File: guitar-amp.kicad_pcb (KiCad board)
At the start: 2 copper layers, 135 x 90 mm, 72 parts, among them J1 Speaker Output, J2 Input, J3 AC Mains, J4 Screw_Terminal_01x02, J5 Screw_Terminal_01x02, J6 Screw_Terminal_01x02, J7 Lamp, SW1 SW_SPST, T1 Transformer_1P_1S

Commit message: Integrate feedback from stackoverflow
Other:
- board text added: "Major issues I immediately see are: 1. For good thermal performance, the board probably should be 50% wider and longer. At the very least. If I was making the board, I'd make it 2x the linear size of your design. Things are too close together for a power amp the way you've laid them out. 2. Electrolytic capacitors should not be anywhere near the vacuum tubes. The tubes get scorching hot - they wi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"
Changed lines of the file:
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@@
     (effects (font (size 1.5 1.5) (thickness 0.3)))
   )
-  (gr_text "Hole Size\n\n- All C and R 0.8\n- Terminal sockets 1\n- Potis 1\n- Valves 1.02\n- Bridge rectifier 1.2\n- Jack socket 1.2\n\n" (at 54.356 97.536) (layer "User.1")
+  (gr_text "Hole Size\n\n- All C and R 0.8\n- Terminal sockets 1\n- Potis 1\n- Valves 1.02\n- Bridge rectifier 1.2\n- Jack socket 1.2\n\n" (at 144 176) (layer "User.1")
     (effects (font (size 1.5 1.5) (thickness 0.3)) (justify left))
   )
+  (gr_text "Major issues I immediately see are:\n\n1. For good thermal performance, the board probably should be 50% wider and longer. At the very least. If I was making the board, I'd make it 2x the linear size of your design. Things are too close together for a power amp the way you've laid them out.\n\n2. Electrolytic capacitors should not be anywhere near the vacuum tubes. The tubes get scorching hot - they will gladly burn your fingers if you touch them just a few minutes from power-up.\n\n   Ideally, you'd want tubes on the top side of the board, and everything else on the bottom side - perhaps connectors included, but I'm not adamant about them.\n\n   Even then, those electrolytics may get warmish from conduction through the tube sockets and PCB. But they should be fine as long as they are 105&deg;C, 8000hours (or more) parts.\n\n3. All the signal/power traces should be on one side of the board - probably the top side, for ease of access in case any post-production {dblquote}surgery{dblquote} is needed. That way they won't be buried under all the passive parts.\n\n   The bottom side should be an almost uninterrupted ground plane, perhaps with one or two short {dblquote}jumper traces{dblquote} to bridge the traces on the signal side that must cross each other. As it stands, the ground plane is highly segmented and won't do its job properly.\n\n4. There should be a star ground point at the bottom of the output tube's cathode RC circuit. The remaining ground plane and the rectifier ground should converge on that point.\n\n   Otherwise, there may be some feedback from the output stage to the preamp stages. Perhaps even the cathode follower and tone control should be included in the sub-plane that defines the star ground. It won't be literally a star, but close: a {dblquote}blob{dblquote} of ground plane separated from the rest of it, with just one connection point.\n\n5. I'm not sure all the resistors are properly rated for power dissipation. You'd want to:\n\n   - go through all the resistors on the schematic and determine their average power dissipation\n   - multiply those dissipations by a factor of 2.5 or 3\n   - choose the next higher dissipation rating for each resistor, mark it on the schematic, and choose footprints accordingly.\n\n   I'm not saying there are problems - I did not check, but that's an important step you must do. Otherwise you'll have problems with resistors that will discolor and scorch the PCB at best, and just burn out at worst.\n\nThere may be other issues - I'll leave them for others to find out (no time at the moment to look further).\n\nOverall, you've done a good job for a (presumably) first project. Addressing the issues above should go a long way towards a circuit that will work on the first try.\n\nAdditional props for using version control. Excellent!\n\nThe soft-start circuit could be refined by using a relay configured to latch on when a pushbutton is pressed, and then open when the power is removed. That way anytime the power is lost, the soft start series resistor will be in series with the cathodes.\n\nAnd mind that anode (plate) voltage. It's out there to kill you. Use an isolation safety transformer to power the amp. The isolated side's earth terminal goes to the center of the secondary winding, or to one of the ends of that winding, and is not connected to earth. The latter would undo the whole point of safety isolation.\n\nhttps://electronics.stackexchange.com/q/663778" (at 0 -49) (layer "User.1")
+    (effects (font (size 1.5 1.5) (thickness 0.3)) (justify left))
+  )

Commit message: Fix R6 and Remove C15
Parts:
- removed C15: 1u / 250V, Capacitor_THT:C_Rect_L27.0mm_W9.0mm_P23.00mm
- moved C11 16.4 mm to (137.0, 85.1)
- moved R14 15.2 mm to (131.3, 85.1), turned to 90 degrees
- moved R10 14.0 mm to (136.1, 99.8)
- moved R6 11.3 mm to (157.0, 115.8), turned to 90 degrees
- moved R13 4.31 mm to (135.3, 115.7)
- moved C5 2.47 mm to (161.5, 109.0)
- moved TP1 0.37 mm to (127.3, 112.7)
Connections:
- R10 pad 2: Net-(C15-Pad1) -> Net-(R10-Pad2)
- R6 pad 2: Net-(C5-Pad2) -> /HighDC_V1B_Anode
- V1 pad 7: Net-(C15-Pad2) -> Net-(R10-Pad2)
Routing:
- net Net-(C15-Pad2): track 16.7 -> 0.00 mm
- net Net-(J2-PadT): track 17.5 -> 25.3 mm
- net Net-(R10-Pad2): track 0.00 -> 6.70 mm
- net /HighDC_V1B_Anode: track 11.9 -> 18.1 mm
- net Net-(C15-Pad1): track 4.68 -> 0.00 mm
- net Net-(C5-Pad2): track 16.4 -> 12.4 mm
- net Net-(C11-Pad1): track 22.5 -> 26.4 mm
- net /HighDC_227VDC: track 48.6 -> 49.6 mm

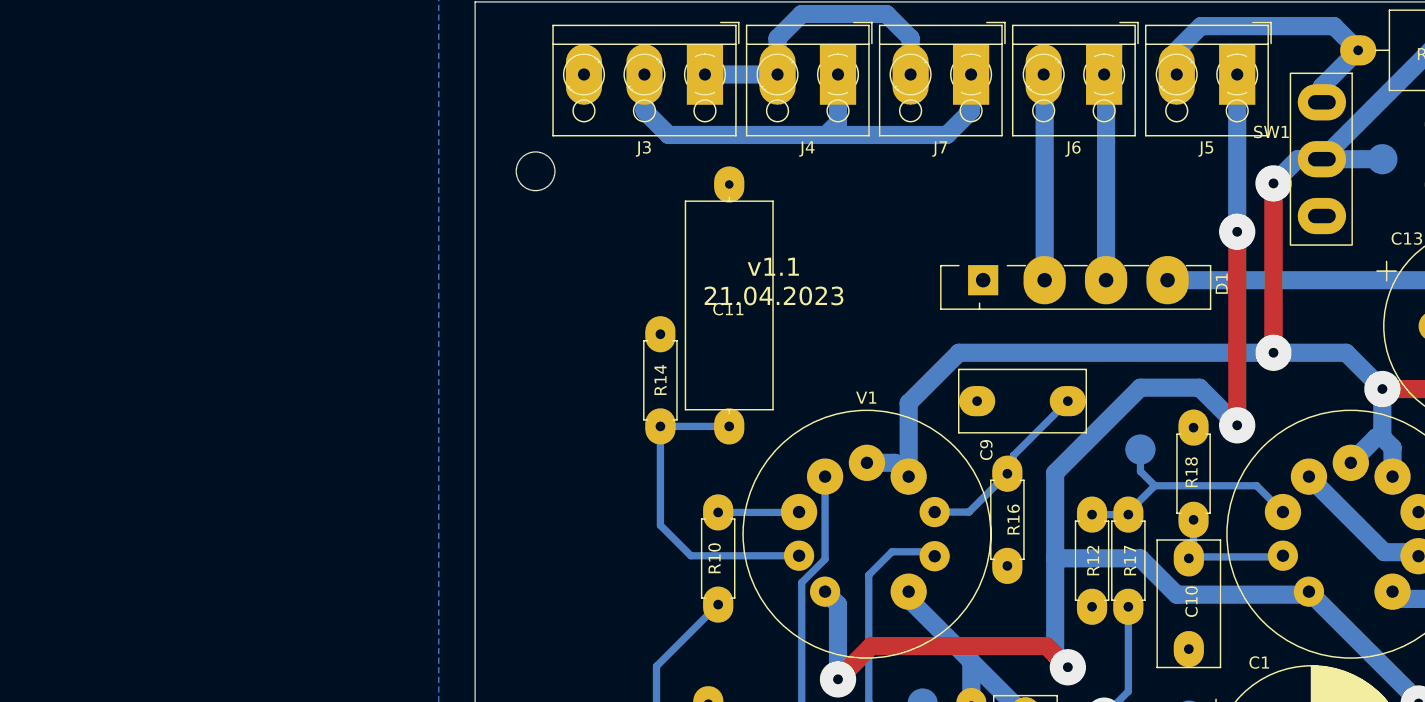
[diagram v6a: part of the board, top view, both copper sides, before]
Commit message: Self latching circuit for soft start
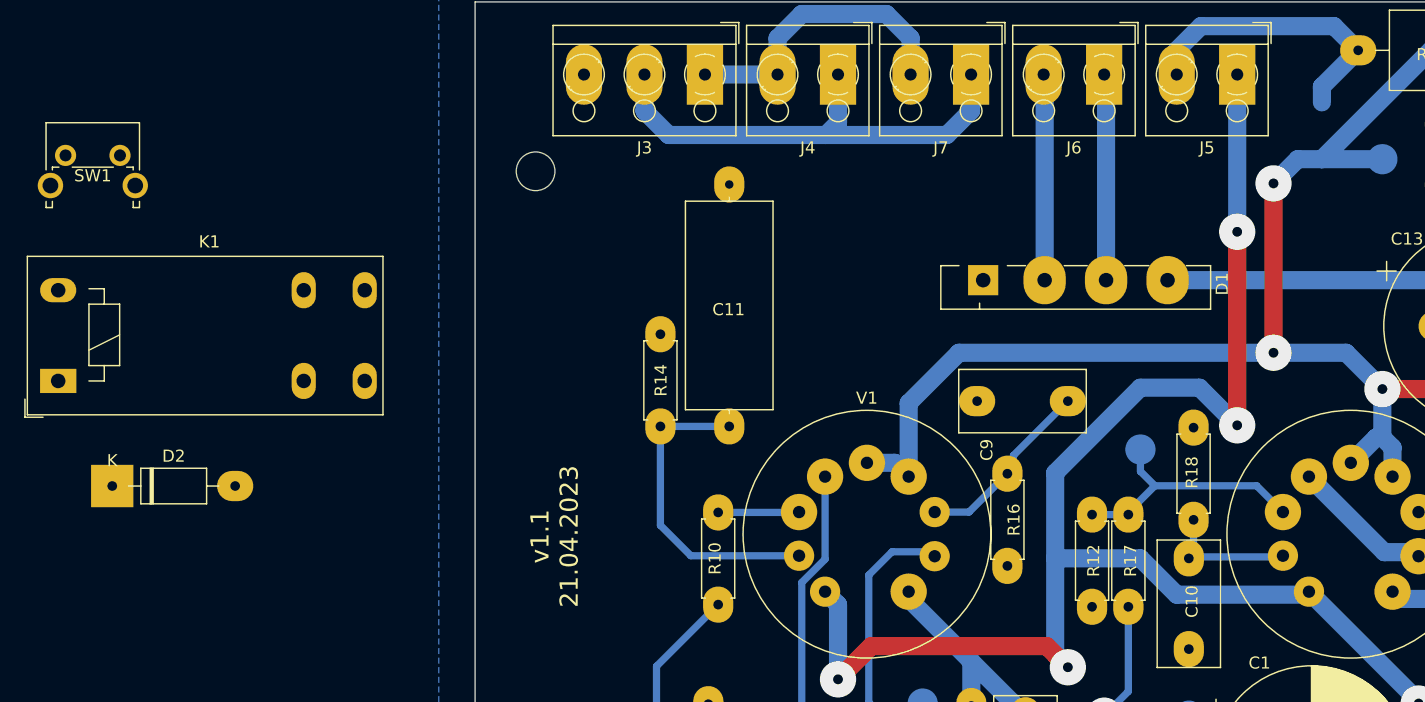
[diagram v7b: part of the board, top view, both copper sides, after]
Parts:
- added D2: UF4001, Diode_THT:D_DO-41_SOD81_P10.16mm_Horizontal, F.Cu at (86.0, 90.0)
- added K1: RT444012, Relay_THT:Relay_DPST_Schrack-RT2-FormA_RM5mm, F.Cu at (81.5, 81.3)
- SW1: value SW_SPST -> SW_Push; footprint Button_Switch_THT:SW_CuK_JS202011CQN_DPDT_Straight -> Button_Switch_THT:SW_Tactile_SPST_Angled_PTS645Vx58-2LFS
- moved SW1 103.9 mm to (82.1, 62.7), turned to 0 degrees
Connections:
- J5 pad 2: /HighCurrentTrace1 -> Net-(J5-Pad2)
- R24 pad 1: /HighCurrentTrace1 -> /HighCurrentTrace2
- R24 pad 2: /HighCurrentTrace2 -> Net-(J5-Pad2)
- SW1 pad 1: /HighCurrentTrace1 -> Net-(K1-Pad11)
- SW1 pad 2: /HighCurrentTrace2 -> Net-(J5-Pad2)
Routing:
- net Net-(J5-Pad2): track 0.00 -> 24.2 mm
- net /HighCurrentTrace1: track 24.2 -> 0.00 mm
